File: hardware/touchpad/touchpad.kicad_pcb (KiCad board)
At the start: 2 copper layers, 194.2 x 134.1 mm, 187 parts, among them J1 Conn_01x26_MountingPin, J10 Conn_02x03_Odd_Even, J100 Conn_02x03_Odd_Even, J101 Conn_02x03_Odd_Even, J102 Conn_02x03_Odd_Even, J103 Conn_02x03_Odd_Even, J104 Conn_02x03_Odd_Even, J105 Conn_02x03_Odd_Even, J106 Conn_02x03_Odd_Even, J107 Conn_02x03_Odd_Even, J108 Conn_02x03_Odd_Even, J109 Conn_02x03_Odd_Even, J11 Conn_02x03_Odd_Even, J110 Conn_02x03_Odd_Even, J111 Conn_02x03_Odd_Even, J112 Conn_02x03_Odd_Even, J113 Conn_02x03_Odd_Even, J114 Conn_02x03_Odd_Even, J115 Conn_02x03_Odd_Even, J116 Conn_02x03_Odd_Even, J117 Conn_02x03_Odd_Even, J118 Conn_02x03_Odd_Even, J119 Conn_02x03_Odd_Even, J12 Conn_02x03_Odd_Even, J120 Conn_02x03_Odd_Even, J121 Conn_02x03_Odd_Even, J122 Conn_02x03_Odd_Even, J123 Conn_02x03_Odd_Even, J124 Conn_02x03_Odd_Even, J125 Conn_02x03_Odd_Even, J126 Conn_02x03_Odd_Even, J127 Conn_02x03_Odd_Even, J128 Conn_02x03_Odd_Even, J129 Conn_02x03_Odd_Even, J13 Conn_02x03_Odd_Even, J130 Conn_02x03_Odd_Even, J131 Conn_02x03_Odd_Even, J132 Conn_02x03_Odd_Even, J133 Conn_02x03_Odd_Even, J134 Conn_02x03_Odd_Even, J135 Conn_02x03_Odd_Even, J136 Conn_02x03_Odd_Even, J137 Conn_02x03_Odd_Even, J138 Conn_02x03_Odd_Even, J139 Conn_02x03_Odd_Even, J14 Conn_02x03_Odd_Even, J140 Conn_02x03_Odd_Even, J141 Conn_02x03_Odd_Even, J142 Conn_02x03_Odd_Even, J143 Conn_02x03_Odd_Even, J144 Conn_02x03_Odd_Even, J145 Conn_02x03_Odd_Even, J146 Conn_02x03_Odd_Even, J147 Conn_02x03_Odd_Even, J148 Conn_02x03_Odd_Even, J149 Conn_02x03_Odd_Even, J15 Conn_02x03_Odd_Even, J150 Conn_02x03_Odd_Even, J151 Conn_02x03_Odd_Even, J152 Conn_02x03_Odd_Even, J153 Conn_02x03_Odd_Even, J154 Conn_02x03_Odd_Even, J155 Conn_02x03_Odd_Even, J156 Conn_02x03_Odd_Even, J157 Conn_02x03_Odd_Even, J158 Conn_02x03_Odd_Even, J159 Conn_02x03_Odd_Even, J16 Conn_02x03_Odd_Even, J160 Conn_02x03_Odd_Even, J161 Conn_02x03_Odd_Even, J162 Conn_02x03_Odd_Even, J163 Conn_02x03_Odd_Even, J164 Conn_02x03_Odd_Even, J165 Conn_02x03_Odd_Even, J166 Conn_02x03_Odd_Even, J167 Conn_02x03_Odd_Even, J168 Conn_02x03_Odd_Even, J169 Conn_02x03_Odd_Even, J17 Conn_02x03_Odd_Even, J170 Conn_02x03_Odd_Even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

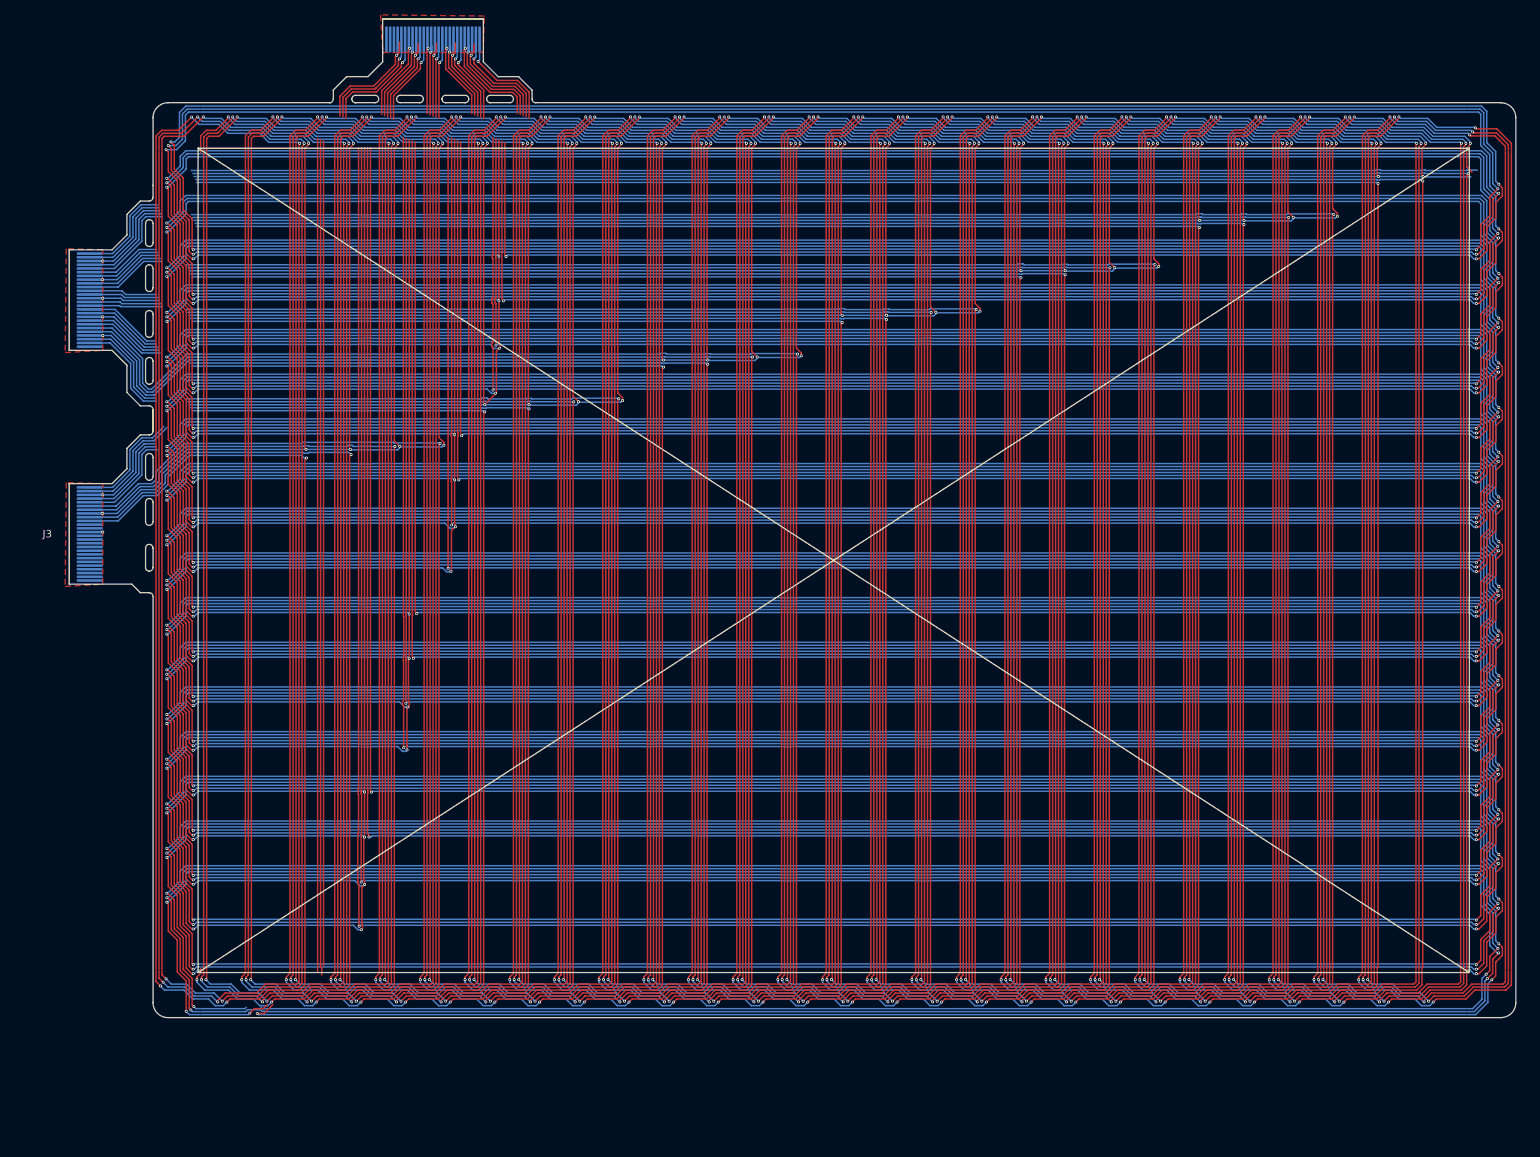
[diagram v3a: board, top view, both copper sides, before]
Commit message: added .2mm spacing
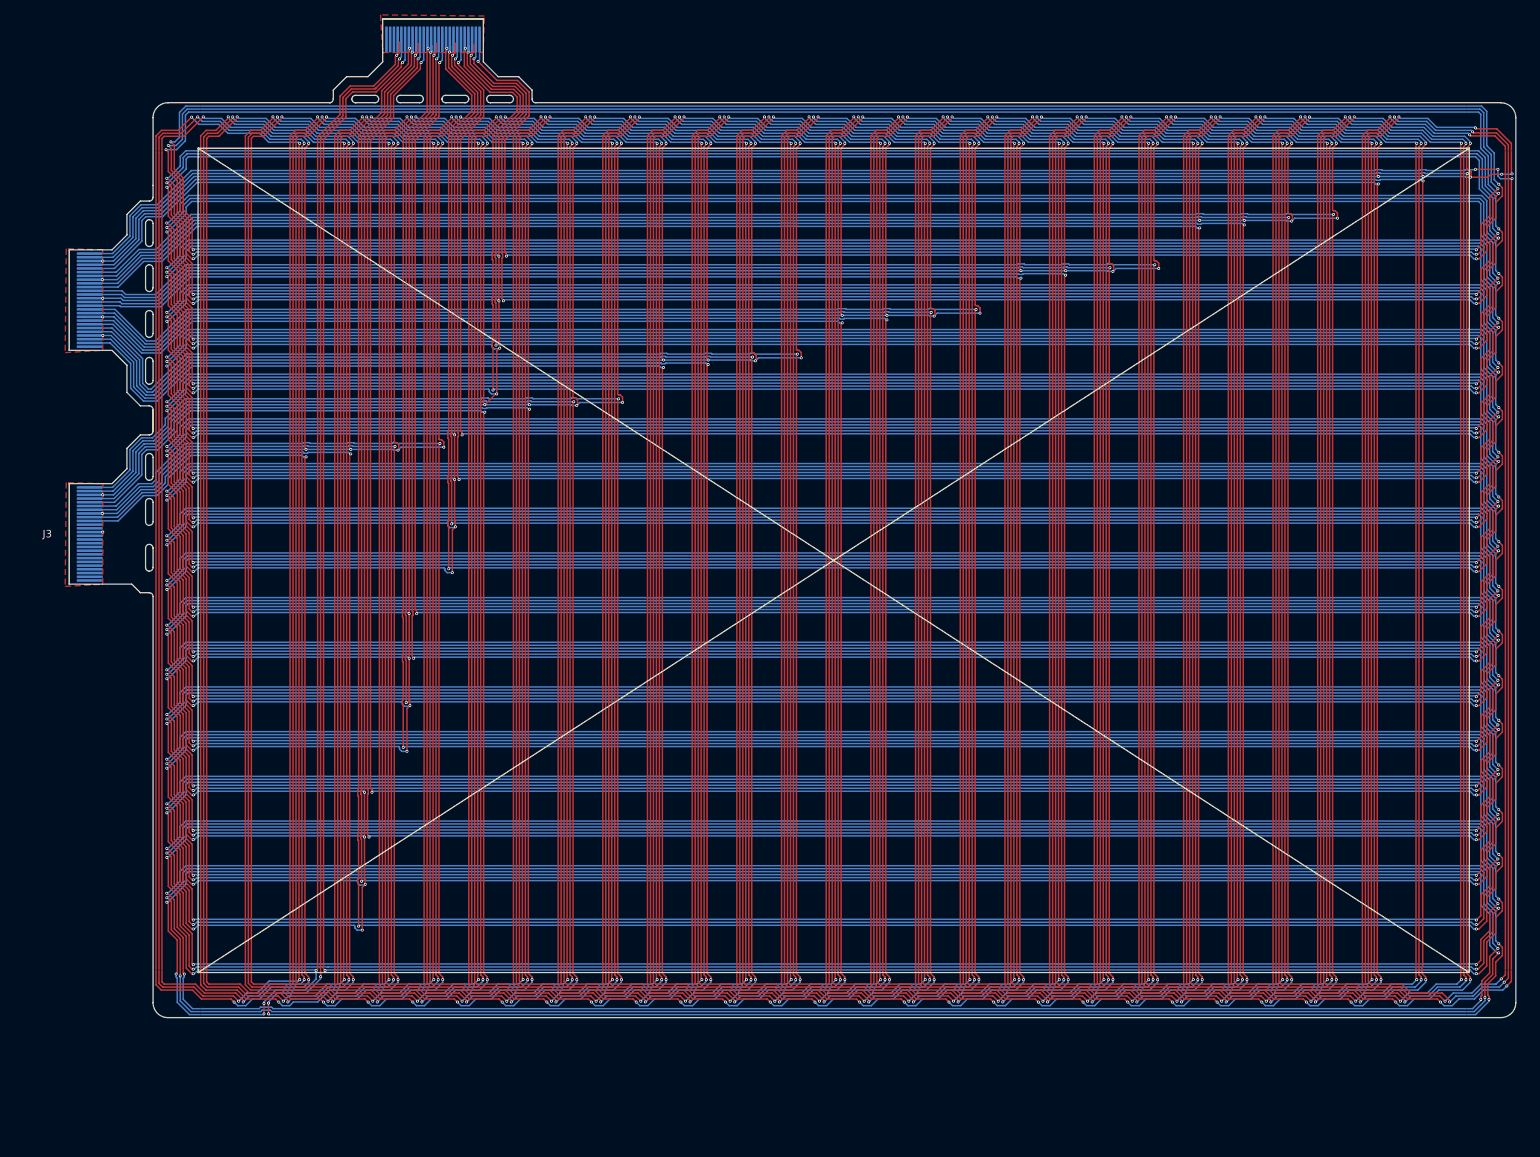
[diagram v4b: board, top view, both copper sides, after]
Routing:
- net /Y16: track 127.6 -> 285.6 mm, vias 1 -> 2
- net Net-(J105-Pin_6): track 0.00 -> 109.4 mm
- net GND: track 2419.2 -> 2517.6 mm, vias 56 -> 61
- net /Y17: track 293.7 -> 304.2 mm, vias 2 -> 4
- net /X0: track 296.6 -> 305.5 mm, vias 0 -> 3
- net /X18: track 165.7 -> 173.4 mm
- net /X22: track 135.1 -> 142.6 mm
- net /X23: track 128.8 -> 136.2 mm
- net /X19: track 159.3 -> 166.1 mm
- net /X6: track 252.6 -> 259.4 mm
- net /X5: track 259.5 -> 266.2 mm
- net /X4: track 266.1 -> 272.7 mm
- net /X7: track 246.3 -> 252.9 mm
- net /X2: track 285.6 -> 292.2 mm
- net /X3: track 279.3 -> 285.8 mm
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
